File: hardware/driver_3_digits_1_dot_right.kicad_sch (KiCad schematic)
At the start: 11 parts, among them U5 HV5622PG

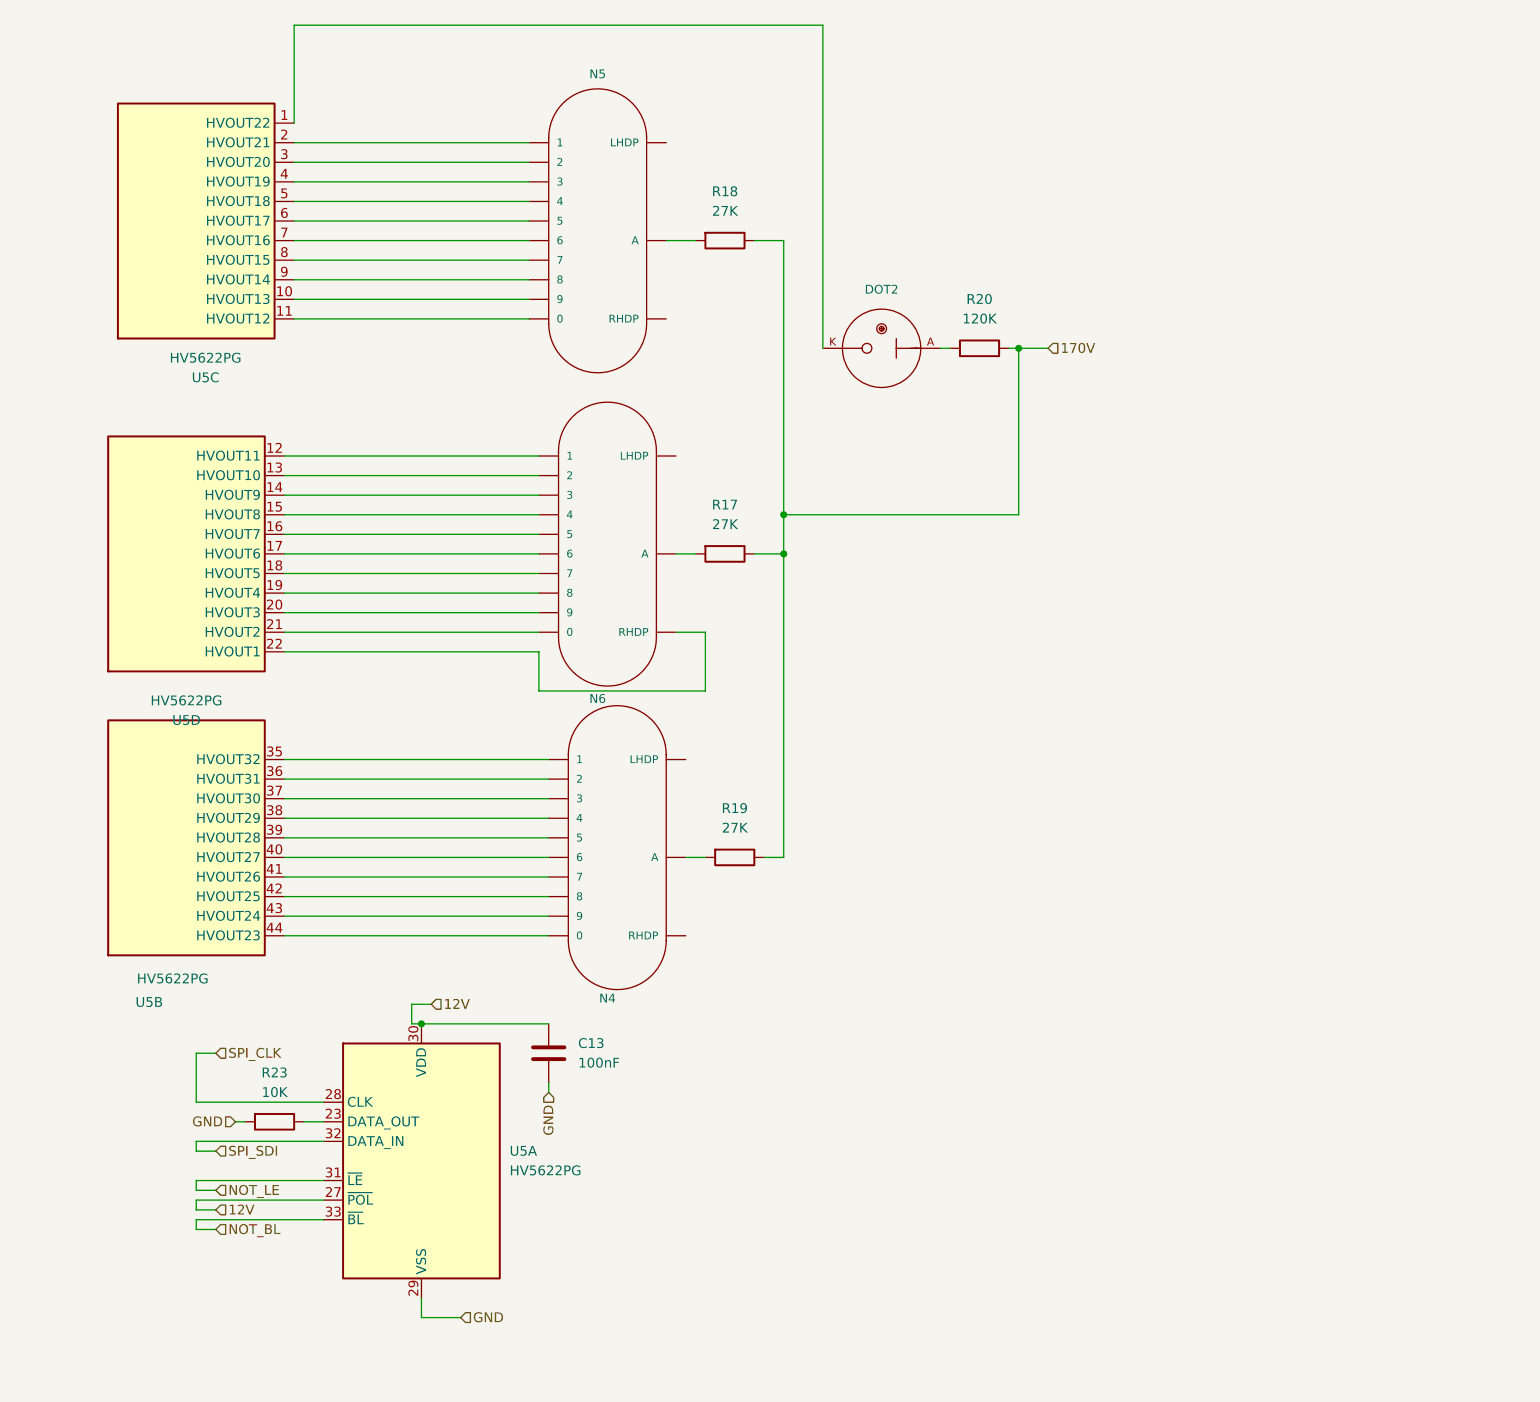
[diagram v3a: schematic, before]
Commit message: Add mosfets for handling levels.
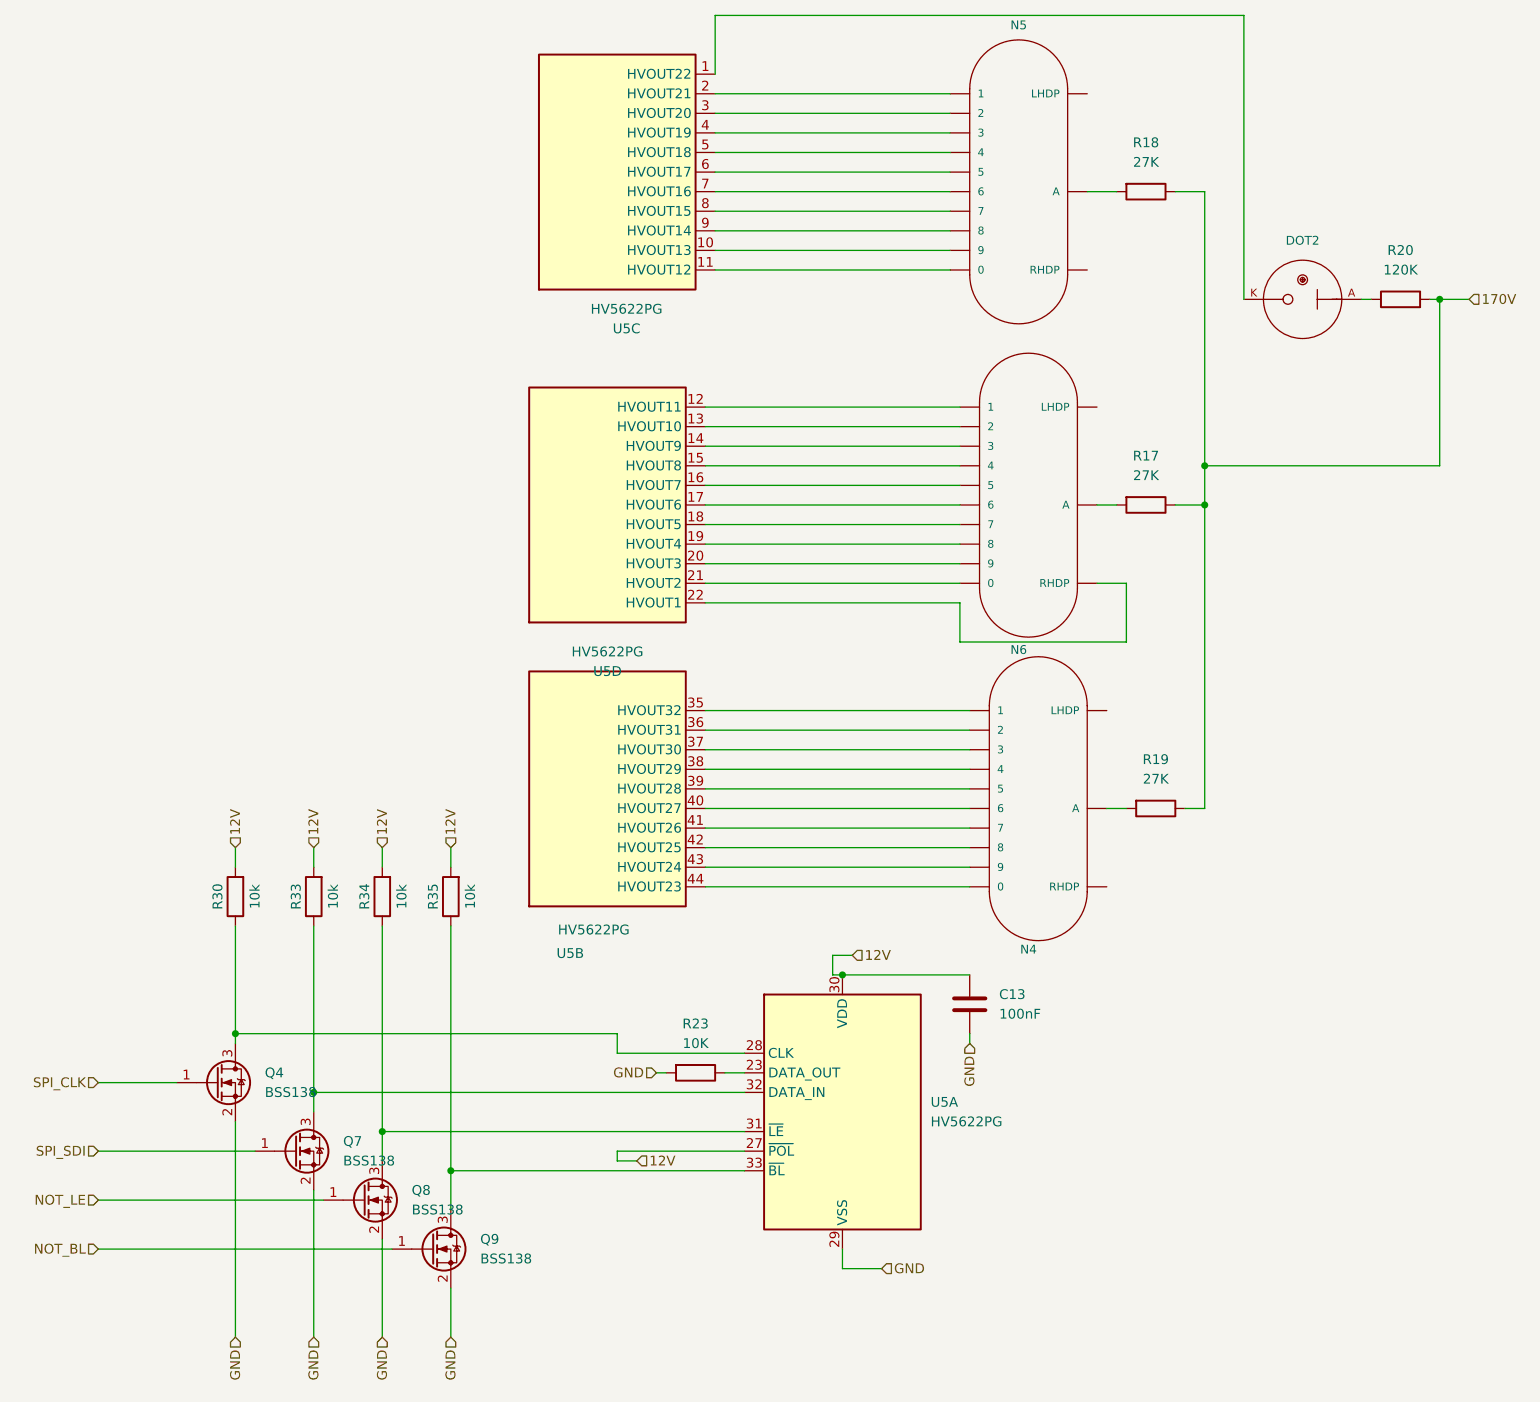
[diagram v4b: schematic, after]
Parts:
- added Q4, Q7, Q8, Q9: BSS138, Package_TO_SOT_SMD:SOT-23, symbol Transistor_FET:BSS138
- added R30, R33, R34, R35: 10k, Resistor_SMD:R_0805_2012Metric, symbol Device:R
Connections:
- net 12V: now also R30.2, R33.2, R34.2, R35.2
- net GND: now also Q4.2 (S), Q7.2 (S), Q8.2 (S), Q9.2 (S)
- net NOT_BL: now also Q9.1 (G); no longer U5.33 (~{BL})
- net NOT_LE: now also Q8.1 (G); no longer U5.31 (~{LE})
- net SPI_CLK: now also Q4.1 (G); no longer U5.28 (CLK)
- net SPI_SDI: now also Q7.1 (G); no longer U5.32 (DATA_IN)
- new net: Q9.3 (D), R35.1, U5.33 (~{BL})
- new net: Q7.3 (D), R33.1, U5.32 (DATA_IN)
- new net: Q8.3 (D), R34.1, U5.31 (~{LE})
- new net: Q4.3 (D), R30.1, U5.28 (CLK)
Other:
- moved on the sheet: C13, DOT2, N4, N5, N6, R17, R18, R19, R20, R23, U5A, U5B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

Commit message: Remove one mosfet on the right since SPI out from the first HV5622 is already on 12v level.
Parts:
- removed Q7: BSS138, Package_TO_SOT_SMD:SOT-23, symbol Transistor_FET:BSS138
- removed R33: 10k, Resistor_SMD:R_0805_2012Metric, symbol Device:R
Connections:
- net SPI_SDI: now also U5.32 (DATA_IN)
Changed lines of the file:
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@@
-	)
-	(junction
-		(at 83.82 158.75)
-		(diameter 0)
-		(color 0 0 0 0)
 	)
 	(junction
@@
 	(wire
 		(pts
-			(xy 55.88 166.37) (xy 76.2 166.37)
-		)
-		(stroke
-			(width 0)
-			(type default)
-		)
-	)
-	(wire
-		(pts
 			(xy 123.19 153.67) (xy 139.7 153.67)
 		)
@@
 	(wire
 		(pts
-			(xy 83.82 158.75) (xy 83.82 161.29)
-		)
-		(stroke
-			(width 0)
-			(type default)
-		)
-	)
-	(wire
-		(pts
 			(xy 55.88 157.48) (xy 66.04 157.48)
 		)
@@
 	(wire
 		(pts
-			(xy 83.82 171.45) (xy 83.82 190.5)
-		)
-		(stroke
-			(width 0)
-			(type default)
-		)
-	)
-	(wire
-		(pts
 			(xy 167.64 100.33) (xy 189.23 100.33)
 		)
@@
 	(wire
 		(pts
-			(xy 83.82 127) (xy 83.82 129.54)
-		)
-		(stroke
-			(width 0)
-			(type default)
-		)
-	)
-	(wire
-		(pts
 			(xy 199.39 77.47) (xy 229.87 77.47)
 		)
@@
 	(wire
 		(pts
-			(xy 83.82 158.75) (xy 139.7 158.75)
-		)
-		(stroke
-			(width 0)
-			(type default)
-		)
-	)
-	(wire
-		(pts
 			(xy 152.4 181.61) (xy 152.4 179.07)
 		)
@@
 	(wire
 		(pts
-			(xy 83.82 137.16) (xy 83.82 158.75)
-		)
-		(stroke
-			(width 0)
-			(type default)
-		)
-	)
-	(wire
-		(pts
 			(xy 134.62 72.39) (xy 167.64 72.39)
 		)
@@
 		(pts
 			(xy 123.19 167.64) (xy 123.19 166.37)
+		)
+		(stroke
+			(width 0)
+			(type default)
+		)
+	)
+	(wire
+		(pts
+			(xy 128.27 158.75) (xy 139.7 158.75)
 		)
 		(stroke
@@
 	(hierarchical_label "SPI_SDI"
 		(shape input)
-		(at 55.88 166.37 180)
+		(at 128.27 158.75 180)
 		(effects
 			(font
@@
 		)
 	)
-	(hierarchical_label "GND"
-		(shape input)
-		(at 83.82 190.5 270)
-		(effects
-			(font
-				(size 1.27 1.27)
-			)
-			(justify right)
-		)
-	)
 	(hierarchical_label "12V"
 		(shape input)
@@
 			)
 			(justify right)
-		)
-	)
-	(hierarchical_label "12V"
-		(shape input)
-		(at 83.82 127 90)
-		(effects
-			(font
-				(size 1.27 1.27)
-			)
-			(justify left)
 		)
 	)
@@
 	(symbol
 		(lib_id "Transistor_FET:BSS138")
-		(at 81.28 166.37 0)
-		(unit 1)
-		(exclude_from_sim no)
-		(in_bom yes)
-		(on_board yes)
-		(dnp no)
-		(fields_autoplaced yes)
-		(property "Reference" "Q7"
-			(at 87.63 165.0999 0)
-			(effects
-				(font
-					(size 1.27 1.27)
-				)
-				(justify left)
-			)
-		)
-		(property "Value" "BSS138"
-			(at 87.63 167.6399 0)
-			(effects
-				(font
-					(size 1.27 1.27)
-				)
-				(justify left)
-			)
-		)
-		(property "Footprint" "Package_TO_SOT_SMD:SOT-23"
-			(at 86.36 168.275 0)
-			(effects
-				(font
-					(size 1.27 1.27)
-					(italic yes)
-				)
-				(justify left)
-				(hide yes)
-			)
-		)
-		(property "Datasheet" "https://www.onsemi.com/pub/Collateral/BSS138-D.PDF"
-			(at 86.36 170.18 0)
-			(effects
-				(font
-					(size 1.27 1.27)
-				)
-				(justify left)
-				(hide yes)
-			)
-		)
-		(property "Description" "50V Vds, 0.22A Id, N-Channel MOSFET, SOT-23"
-			(at 81.28 166.37 0)
-			(effects
-				(font
-					(size 1.27 1.27)
-				)
-				(hide yes)
-			)
-		)
-		(pin "1"
-		)
-		(pin "3"
-		)
-		(pin "2"
-		)
-		(instances
-			(project "nixie_clock"
-				(path "/90430e5f-7049-4de8-b92d-f897c4a89819/fe830805-1f17-45c2-a3b2-c398af349661"
-					(reference "Q7")
-					(unit 1)
-				)
-			)
-		)
-	)
-	(symbol
-		(lib_id "Transistor_FET:BSS138")
 		(at 90.17 172.72 0)
 		(unit 1)
@@
 					(unit 1)
 				)
-			)
-		)
-	)
-	(symbol
-		(lib_id "Device:R")
-		(at 83.82 133.35 180)
-		(unit 1)
-		(exclude_from_sim no)
-		(in_bom yes)
-		(on_board yes)
-		(dnp no)
-		(property "Reference" "R33"
-			(at 81.534 133.35 90)
-			(effects
-				(font
-					(size 1.27 1.27)
-				)
-			)
-		)
-		(property "Value" "10k"
-			(at 86.36 133.35 90)
-			(effects
-				(font
-					(size 1.27 1.27)
-				)
-			)
-		)
-		(property "Footprint" "Resistor_SMD:R_0805_2012Metric"
-			(at 85.598 133.35 90)
-			(effects
-				(font
-					(size 1.27 1.27)
-				)
-				(hide yes)
-			)
-		)
-		(property "Datasheet" "~"
-			(at 83.82 133.35 0)
-			(effects
-				(font
-					(size 1.27 1.27)
-				)
-				(hide yes)
-			)
-		)
-		(property "Description" "Bootmode"
-			(at 89.408 137.414 0)
-			(effects
-				(font
-					(size 1.27 1.27)
-				)
-				(hide yes)
-			)
-		)
-		(pin "1"
-		)
-		(pin "2"
-		)
-		(instances
-			(project "nixie_clock"
-				(path "/90430e5f-7049-4de8-b92d-f897c4a89819/fe830805-1f17-45c2-a3b2-c398af349661"
-					(reference "R33")
-					(unit 1)
-				)
